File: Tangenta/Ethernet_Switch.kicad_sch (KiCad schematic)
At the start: 31 parts, among them J20 Conn_01x08_Pin, U18 RTL8367S-CG, X2 X322525MOB4SI

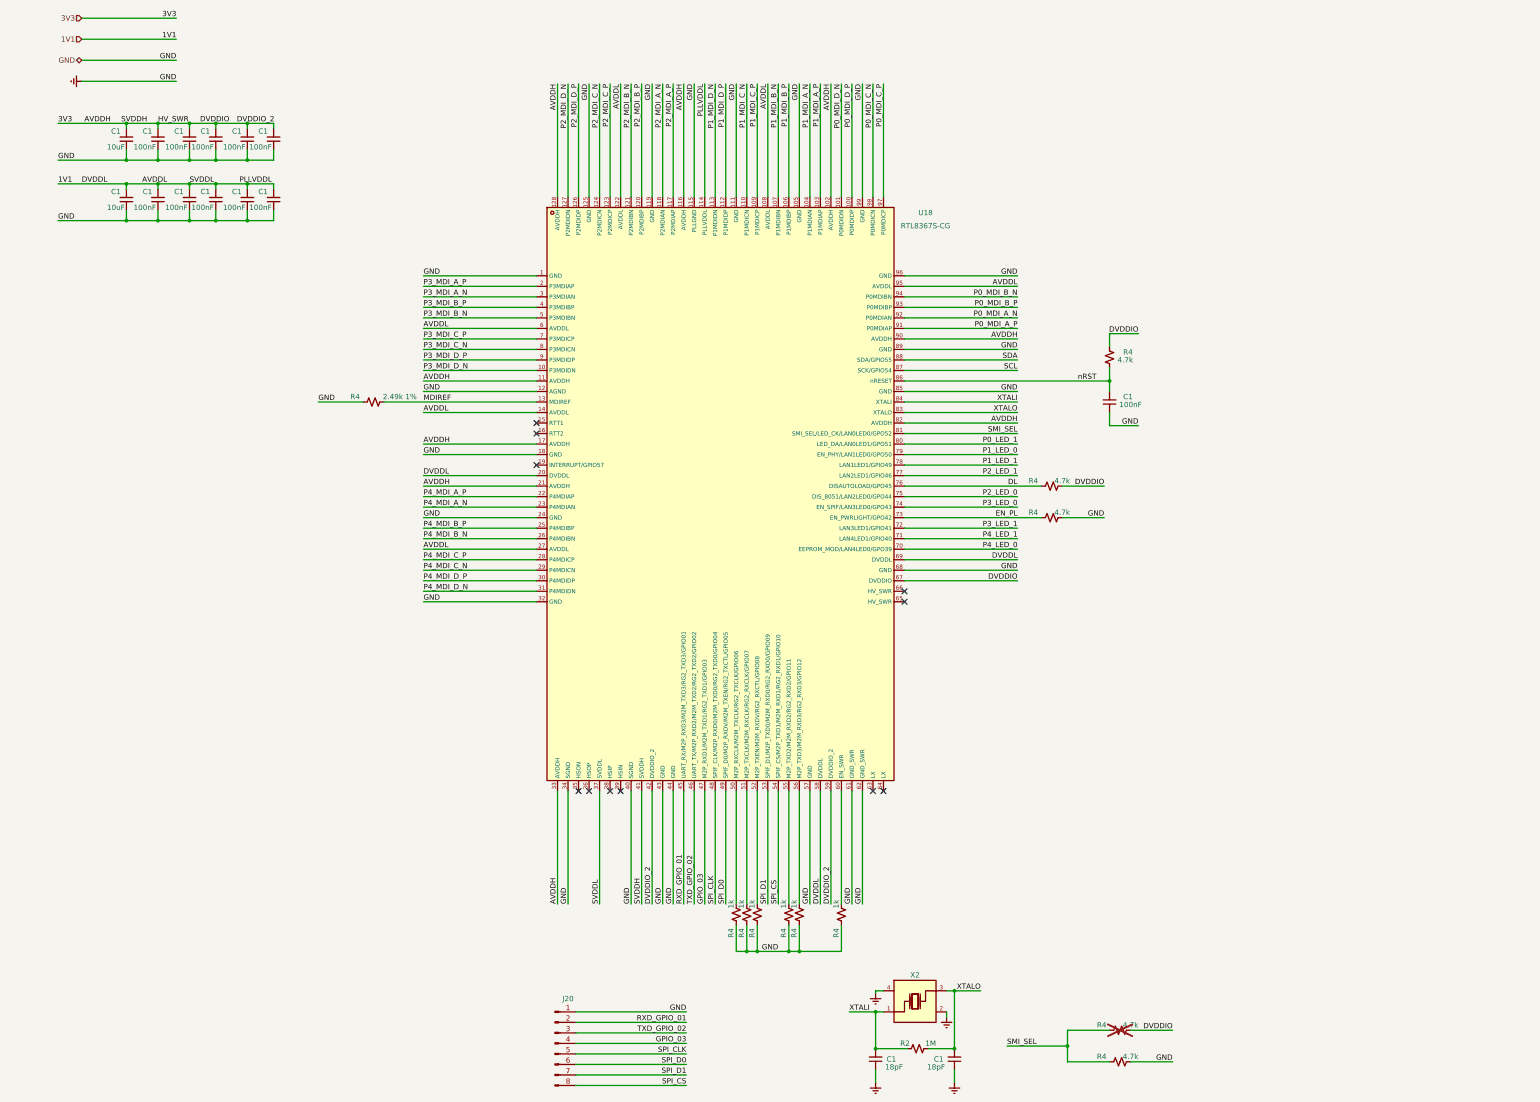
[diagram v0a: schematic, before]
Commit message: Ethernet Switch schematic done, ports TBD...
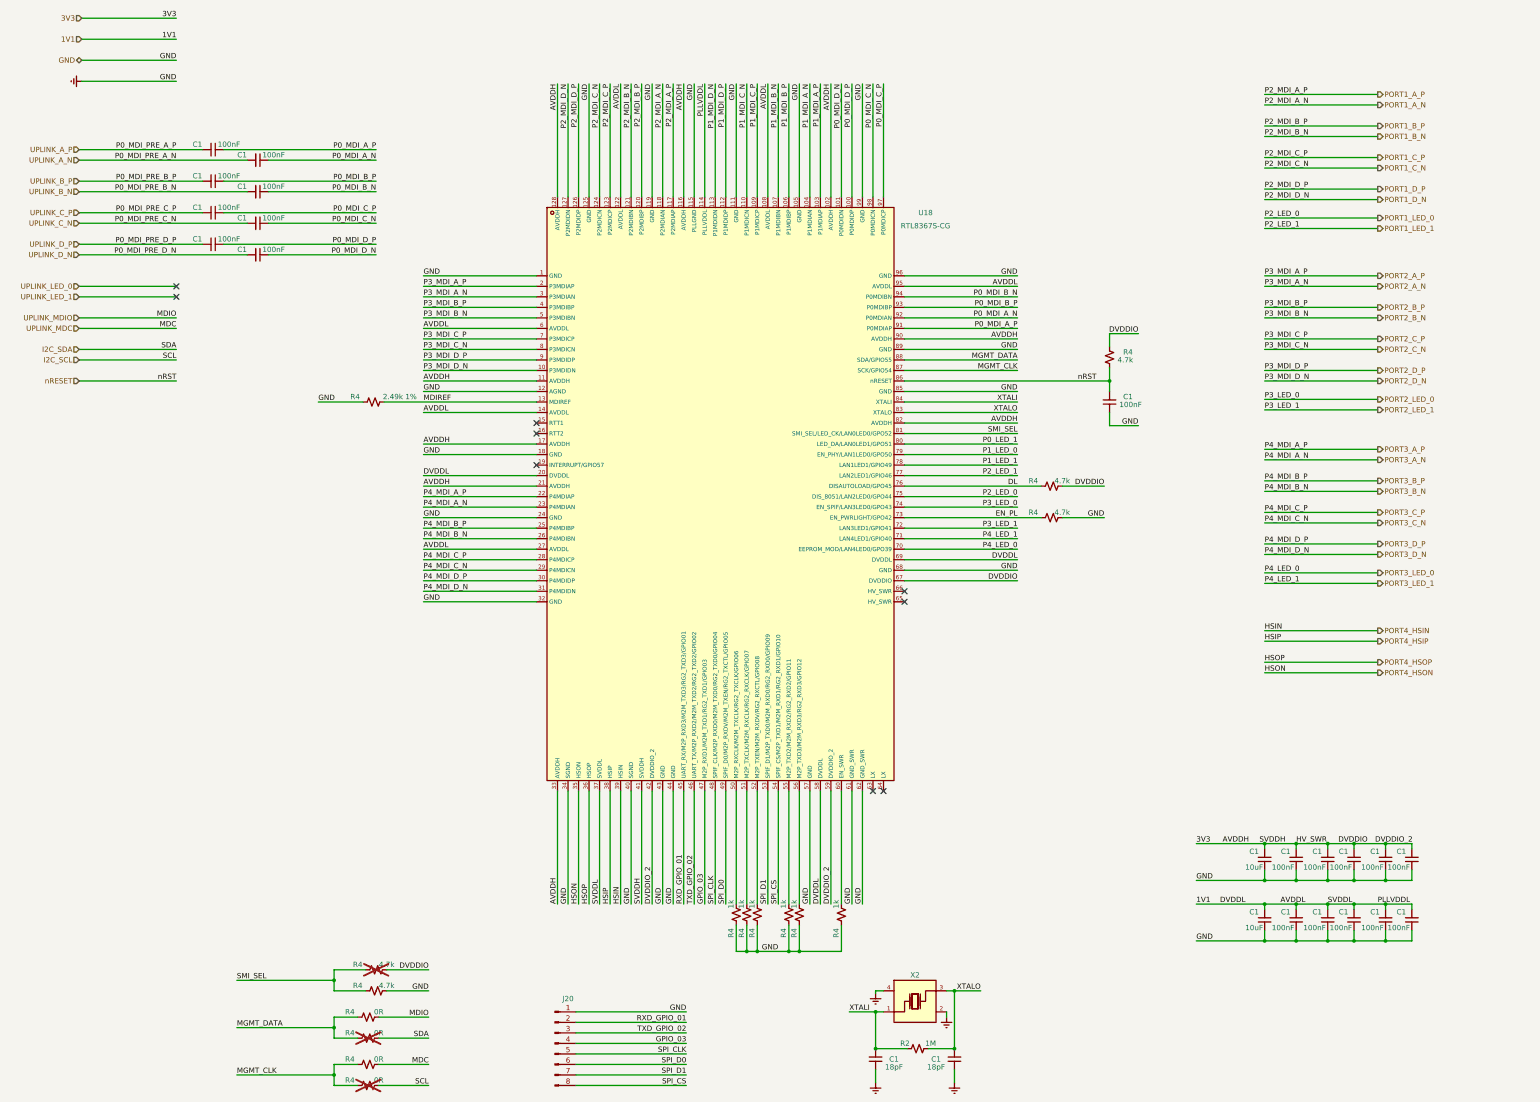
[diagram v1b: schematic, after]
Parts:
- added C1 (x8): 100nF, Capacitor_SMD:C_0402_1005Metric, symbol Device:C_Small
- added R4 (x4): 0R, Resistor_SMD:R_0402_1005Metric, symbol Device:R_Small_US
- R4: footprint Resistor_SMD:R_0603_1608Metric -> Resistor_SMD:R_0402_1005Metric
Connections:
- net P0_MDI_A_N: now also C1.1
- net P0_MDI_A_P: now also C1.1
- net P0_MDI_B_N: now also C1.1
- net P0_MDI_B_P: now also C1.1
- net P0_MDI_C_N: now also C1.1
- net P0_MDI_C_P: now also C1.1
- net P0_MDI_D_N: now also C1.1
- net P0_MDI_D_P: now also C1.1
- net PORT4_HSON: now reaches U18.35 (HSON)
- net PORT4_HSOP: now reaches U18.36 (HSOP)
- net PORT4_HSIP: now reaches U18.38 (HSIP)
- net PORT4_HSIN: now reaches U18.39 (HSIN)
- net P2_LED_0 renamed PORT1_LED_0
- net P2_LED_1 renamed PORT1_LED_1
- net P2_MDI_A_N renamed PORT1_A_N
- net P2_MDI_A_P renamed PORT1_A_P
- net P2_MDI_B_N renamed PORT1_B_N
- net P2_MDI_B_P renamed PORT1_B_P
- net P2_MDI_C_N renamed PORT1_C_N
- net P2_MDI_C_P renamed PORT1_C_P
- net P2_MDI_D_N renamed PORT1_D_N
- net P2_MDI_D_P renamed PORT1_D_P
- net P3_LED_0 renamed PORT2_LED_0
- net P3_LED_1 renamed PORT2_LED_1
- net P3_MDI_A_N renamed PORT2_A_N
- net P3_MDI_A_P renamed PORT2_A_P
- net P3_MDI_B_N renamed PORT2_B_N
- net P3_MDI_B_P renamed PORT2_B_P
- net P3_MDI_C_N renamed PORT2_C_N
- net P3_MDI_C_P renamed PORT2_C_P
- net P3_MDI_D_N renamed PORT2_D_N
- net P3_MDI_D_P renamed PORT2_D_P
- net P4_LED_0 renamed PORT3_LED_0
- net P4_LED_1 renamed PORT3_LED_1
- net P4_MDI_A_N renamed PORT3_A_N
- net P4_MDI_A_P renamed PORT3_A_P
- net P4_MDI_B_N renamed PORT3_B_N
- net P4_MDI_B_P renamed PORT3_B_P
- net P4_MDI_C_N renamed PORT3_C_N
- net P4_MDI_C_P renamed PORT3_C_P
- net P4_MDI_D_N renamed PORT3_D_N
- net P4_MDI_D_P renamed PORT3_D_P
- net SCL renamed MGMT_CLK
- net MGMT_CLK: now also R4.1, R4.1
- net SDA renamed MGMT_DATA
- net MGMT_DATA: now also R4.1, R4.1
- net nRST renamed nRESET
- new net I2C_SCL: R4.2
- new net I2C_SDA: R4.2
- new net UPLINK_A_N: C1.2
- new net UPLINK_A_P: C1.2
- new net UPLINK_B_N: C1.2
- new net UPLINK_B_P: C1.2
- new net UPLINK_C_N: C1.2
- new net UPLINK_C_P: C1.2
- new net UPLINK_D_N: C1.2
- new net UPLINK_D_P: C1.2
- new net UPLINK_MDC: R4.2
- new net UPLINK_MDIO: R4.2
- no-connect marks 11 -> 9
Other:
- moved on the sheet: C1, R4

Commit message: Ethernet, current progress...
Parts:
- added R4: 4.7k, Resistor_SMD:R_0402_1005Metric, symbol Device:R_Small_US
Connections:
- net 3V3: now also R4.2
- net P1_LED_0: now also R4.1
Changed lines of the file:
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@@
     (stroke (width 0) (type default))
   )
+  (wire (pts (xy 267.335 123.19) (xy 277.495 123.19))
+    (stroke (width 0) (type default))
+  )
   (wire (pts (xy 29.845 72.39) (xy 59.69 72.39))
     (stroke (width 0) (type default))
@@
     (stroke (width 0) (type default))
   )
-  (wire (pts (xy 229.235 123.19) (xy 256.54 123.19))
+  (wire (pts (xy 229.235 123.19) (xy 262.255 123.19))
     (stroke (width 0) (type default))
   )
@@
     (effects (font (size 1.27 1.27)) (justify left bottom))
   )
+  (label "DVDDIO" (at 277.495 123.19 180) (fields_autoplaced)
+    (effects (font (size 1.27 1.27)) (justify right bottom))
+  )
   (label "P4_MDI_D_P" (at 316.23 144.78 0) (fields_autoplaced)
     (effects (font (size 1.27 1.27)) (justify left bottom))
@@
         )
       )
+    )
+  )
+  (symbol (lib_id "Device:R_Small_US") (at 264.795 123.19 90) (unit 1)
+    (in_bom yes) (on_board yes) (dnp no)
+    (property "Reference" "R4" (at 260.35 121.92 90)
+      (effects (font (size 1.27 1.27)))
+    )
+    (property "Value" "4.7k" (at 267.335 121.92 90)
+      (effects (font (size 1.27 1.27)))
+    )
+    (property "Footprint" "Resistor_SMD:R_0402_1005Metric" (at 264.795 123.19 0)
+      (effects (font (size 1.27 1.27)) hide)
+    )
+    (property "Datasheet" "~" (at 264.795 123.19 0)
+      (effects (font (size 1.27 1.27)) hide)
+    )
+    (pin "1")
+    (pin "2")
+    (instances
+      (project "Tangenta"
+        (path "/358d1bcf-7599-4352-8c4d-baa18a5f09e6/8215796b-9611-4f43-bcc5-319f8414b8a6"
+          (reference "R4") (unit 1)
+        )
+        (path "/358d1bcf-7599-4352-8c4d-baa18a5f09e6/2bb52479-7b35-496d-9807-27e706c6ef7b"
+          (reference "R127") (unit 1)
+        )
+        (path "/358d1bcf-7599-4352-8c4d-baa18a5f09e6/2bb52479-7b35-496d-9807-27e706c6ef7b/c653b84e-94ee-4be9-b47c-8c767f88973e"
+          (reference "R137") (unit 1)
+        )
+      )

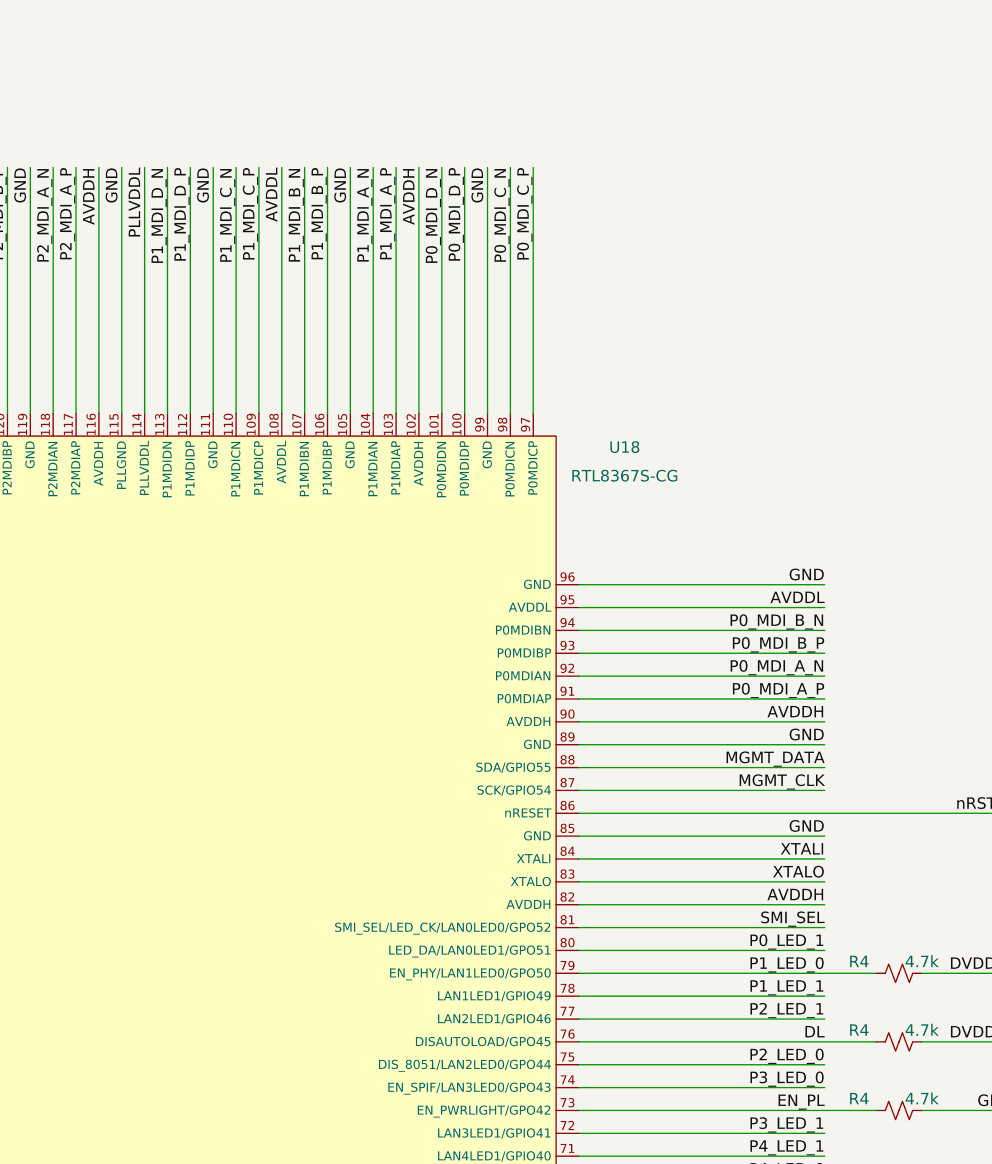
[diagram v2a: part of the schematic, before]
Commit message: Assigned Eth netclasses, MDIO and Toradex connections.
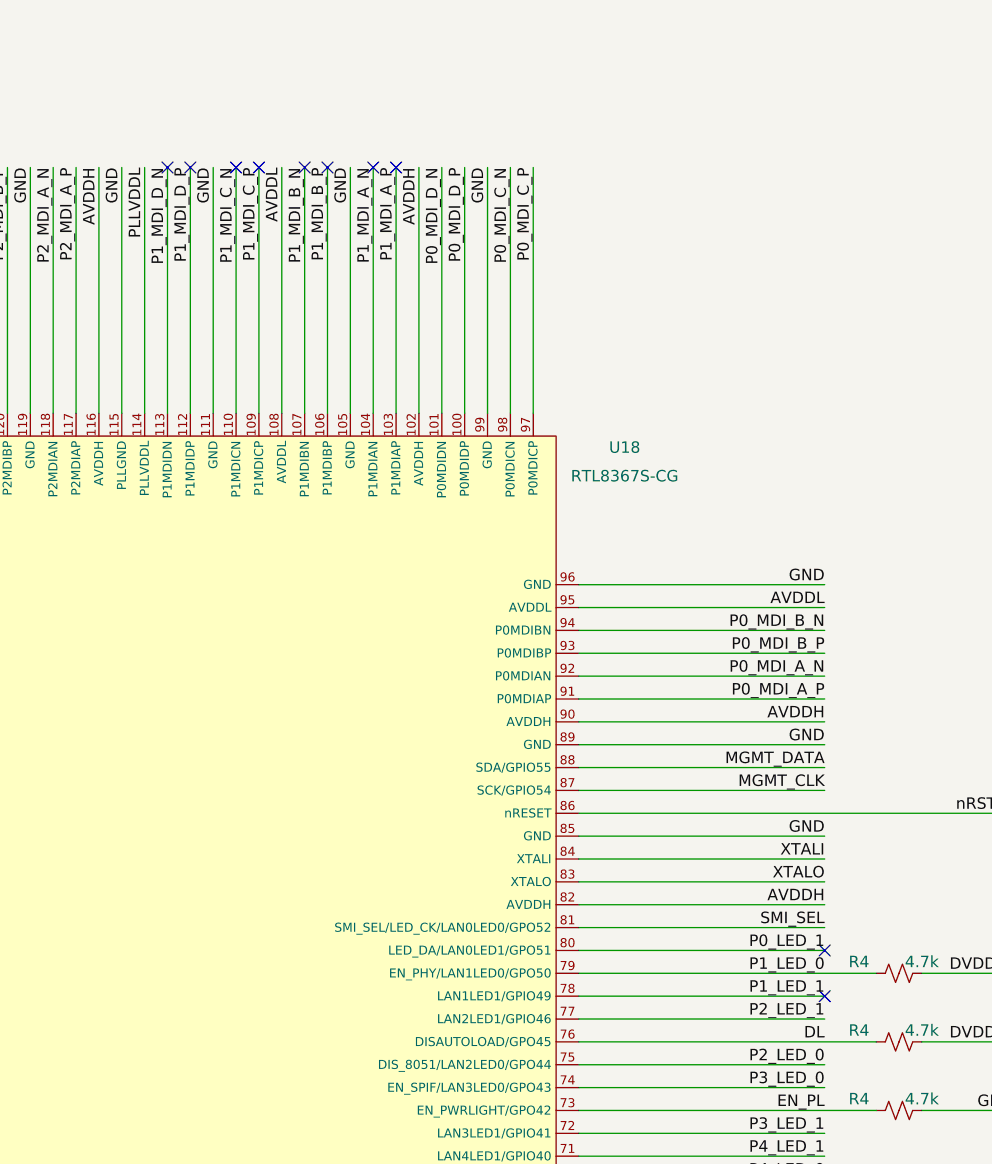
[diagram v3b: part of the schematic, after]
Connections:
- no-connect marks 9 -> 19
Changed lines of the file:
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@@
   )
   (no_connect (at 221.615 204.47))
+  (no_connect (at 186.055 33.655))
+  (no_connect (at 201.295 33.655))
+  (no_connect (at 191.135 33.655))
+  (no_connect (at 193.675 33.655))
   (no_connect (at 53.34 82.55))
+  (no_connect (at 256.54 120.65))
   (no_connect (at 229.235 158.75))
   (no_connect (at 140.335 118.11))
+  (no_connect (at 183.515 33.655))
   (no_connect (at 229.235 156.21))
   (no_connect (at 140.335 115.57))
+  (no_connect (at 208.915 33.655))
   (no_connect (at 140.335 125.73))
+  (no_connect (at 256.54 125.73))
   (no_connect (at 53.34 85.09))
   (no_connect (at 224.155 204.47))
+  (no_connect (at 206.375 33.655))
+  (no_connect (at 198.755 33.655))
   (wire (pts (xy 140.335 90.17) (xy 113.03 90.17))
     (stroke (width 0) (type default))

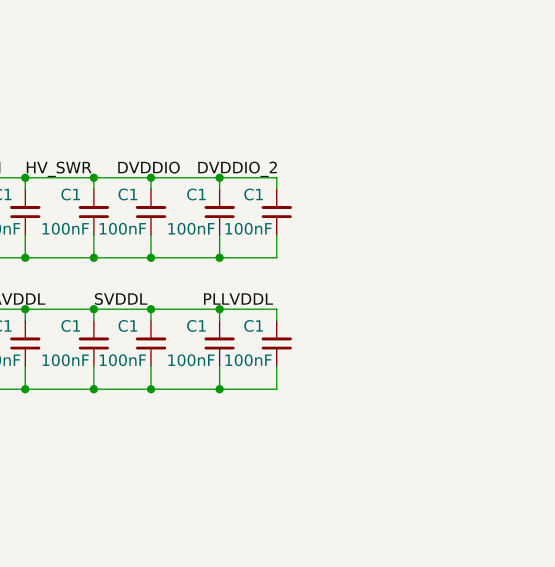
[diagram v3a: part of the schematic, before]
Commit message: Enhanced power delivery to the Ethernet SW.
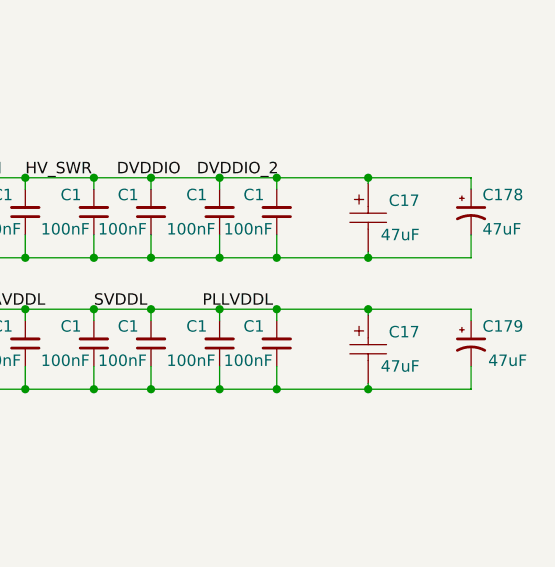
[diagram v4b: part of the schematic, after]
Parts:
- added C17 (x2): 47uF, CAP_TANTAL_A:CAP_TANTAL_A, symbol CAP_TANTAL_A:CA45-A-6_3V-47UF-K
- added C178, C179: 47uF, CAP_L5:CAP_L5, symbol CAP_L5:16CE47FSS
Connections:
- net 1V1: now also C17.1, C179.1
- net 3V3: now also C17.1, C178.1
- net GNDREF: now also C17.2, C17.2, C178.2, C179.2

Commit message: Libraries exported from global to project.
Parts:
- C1: symbol Device:C_Small -> CholaSymbolsPrjLib:C_Small
- C17: symbol CAP_TANTAL_A:CA45-A-6_3V-47UF-K -> CholaSymbolsPrjLib:CA45-A-6_3V-47UF-K
- C178, C179: symbol CAP_L5:16CE47FSS -> CholaSymbolsPrjLib:16CE47FSS
- J20: symbol Connector:Conn_01x08_Pin -> CholaSymbolsPrjLib:Conn_01x08_Pin
- R2, R4: symbol Device:R_Small_US -> CholaSymbolsPrjLib:R_Small_US
- U18: symbol RTL8367S_CG:RTL8367S-CG -> CholaSymbolsPrjLib:RTL8367S-CG
- X2: symbol XTAL_25MHZ:X322525MOB4SI -> CholaSymbolsPrjLib:X322525MOB4SI

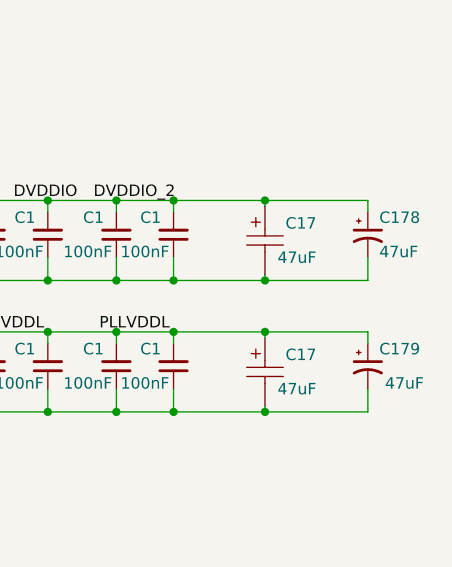
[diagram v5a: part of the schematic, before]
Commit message: Re-annotated. Ready for JLCPCB design verification.
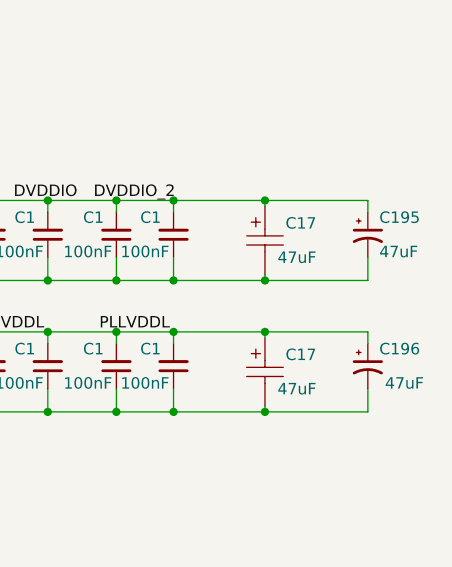
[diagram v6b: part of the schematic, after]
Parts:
- renumbered C178 to C195, C179 to C196

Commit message: initialize branch
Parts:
- renumbered C1 to C170, C1 to C171, C1 to C172, C1 to C173, C1 to C174, C1 to C175, C1 to C176, C1 to C177, C1 to C178, C1 to C179, C1 to C180, C1 to C181, C1 to C182, C1 to C183, C1 to C184, C1 to C185, C1 to C186, C1 to C187, C1 to C188, C1 to C189, C1 to C190, C1 to C191, C1 to C192, C17 to C193, C17 to C194, J20 to J26, R4 to R152, R4 to R153, R4 to R154, R4 to R155, R4 to R156, R4 to R157, R4 to R158, R4 to R159, R4 to R160, R4 to R161, R4 to R162, R4 to R163, R4 to R164, R2 to R165, R4 to R166, R4 to R167, R4 to R168, R4 to R169, U18 to U21

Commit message: J6-J8,J22-J25,S1,U21
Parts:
- U21: footprint RTL8367S_CG:RTL8367S-CG -> CholaFootprintsPrjLib:RTL8367S-CG
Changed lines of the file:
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@@
       (effects (font (size 1.27 1.27)))
     )
-    (property "Footprint" "RTL8367S_CG:RTL8367S-CG" (at 184.785 143.51 0)
+    (property "Footprint" "CholaFootprintsPrjLib:RTL8367S-CG" (at 184.785 143.51 0)
       (effects (font (size 1.27 1.27) italic) hide)
     )
